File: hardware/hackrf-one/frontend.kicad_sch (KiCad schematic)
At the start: 150 parts, among them J10 GND_CLIP, J2 RF-SHIELD-FRAME, J3 RF-SHIELD-COVER, J4 MOUNTING_HOLE, J5 MOUNTING_HOLE, J6 MOUNTING_HOLE, J7 MOUNTING_HOLE, J8 MOUNTING_HOLE, J9 MOUNTING_HOLE, P13 GPO1, P17 GPO6, P19 GPO3, P21 REF_IN, P27 MIXER_SDATA, P31 MIXER_SCLK, P32 MIXER_ENX, P33 MIXER_RESETX, P34 MIX_BYPASS, P35 !MIX_BYPASS, P4 ANTENNA, P43 RX, P44 HP, P45 LP, P46 TX_MIX_BP, P47 RX_MIX_BP, P48 TX_AMP, P49 RX_AMP, P50 AMP_BYPASS, P51 !TX_AMP_PWR, P52 !RX_AMP_PWR, P6 GPO4, P7 GPO2, Q4 BSS84, T1 MIX_IN_BALUN, T2 MIX_OUT_BALUN, U1 SKY13453, U10 SKY13453, U11 SKY13453, U12 SKY13317, U13 TRF37B73, U14 SKY13317, U2 SKY13453, U25 TRF37B73, U3 RX_LOWPASS_FILTER, U4 RFFC5072, U5 SKY13453, U6 SKY13453, U7 SKY13453, U8 RX_HIGHPASS_FILTER, U9 SKY13317

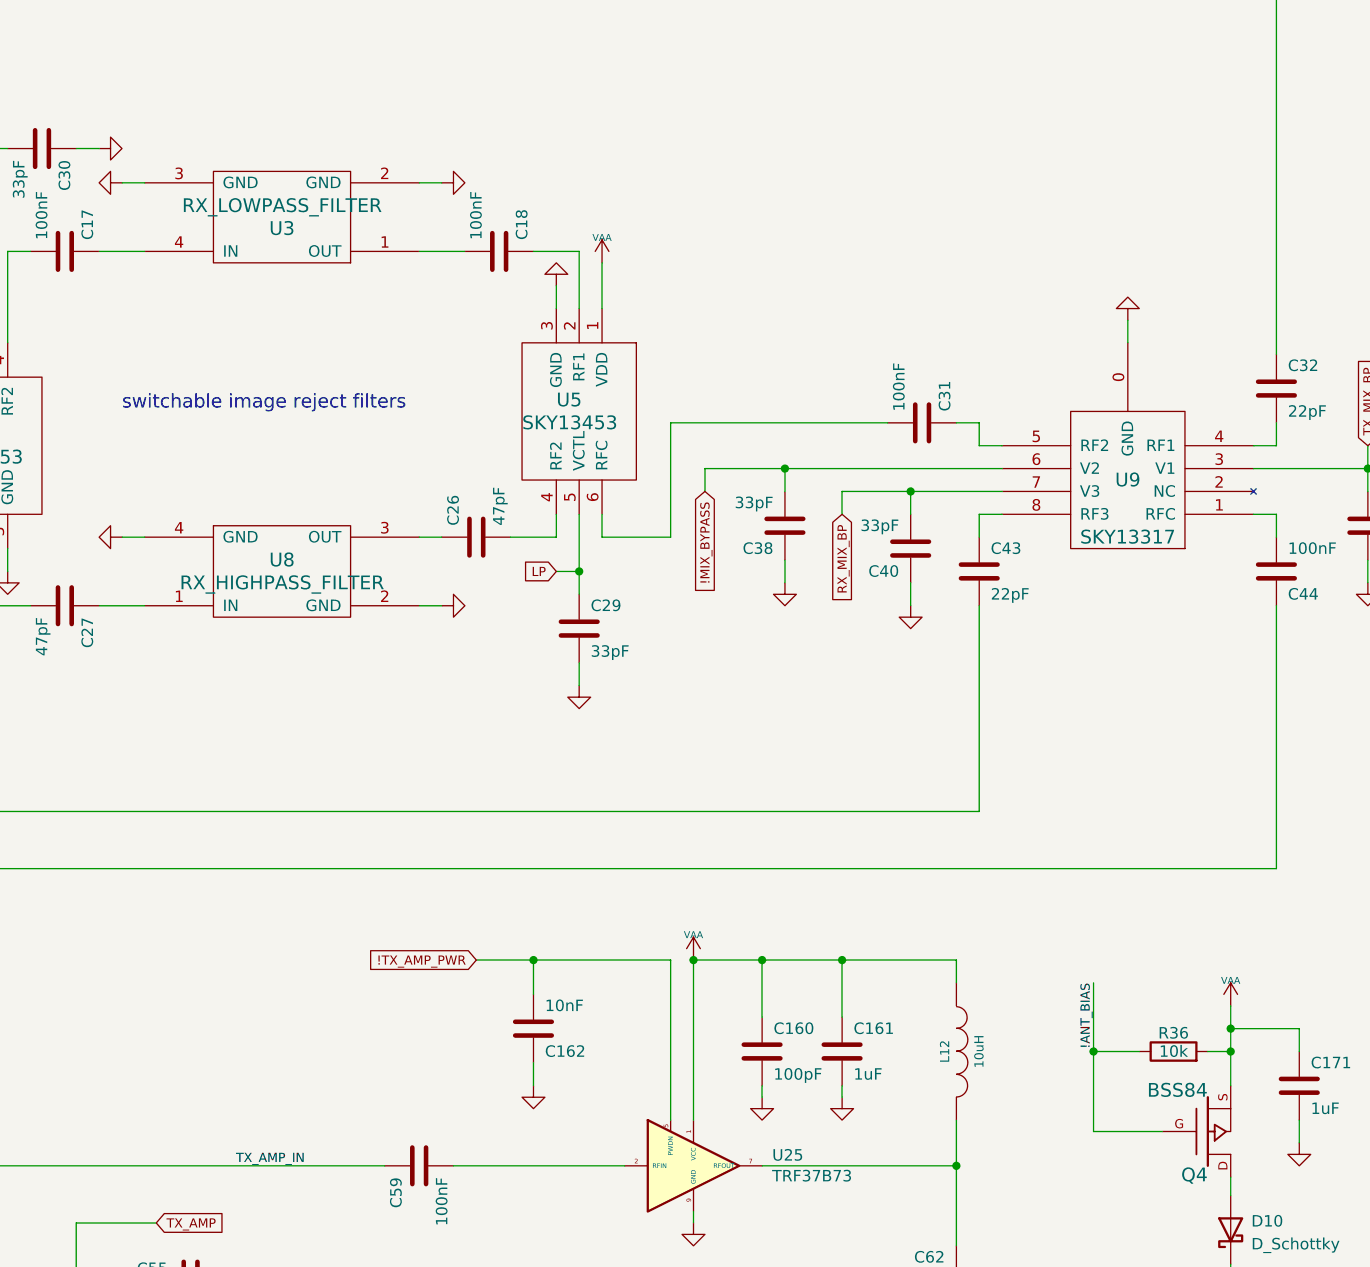
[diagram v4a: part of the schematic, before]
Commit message: Made design changes to indicate version 15. Correct Q3/4/5 part-no and LPF rotation
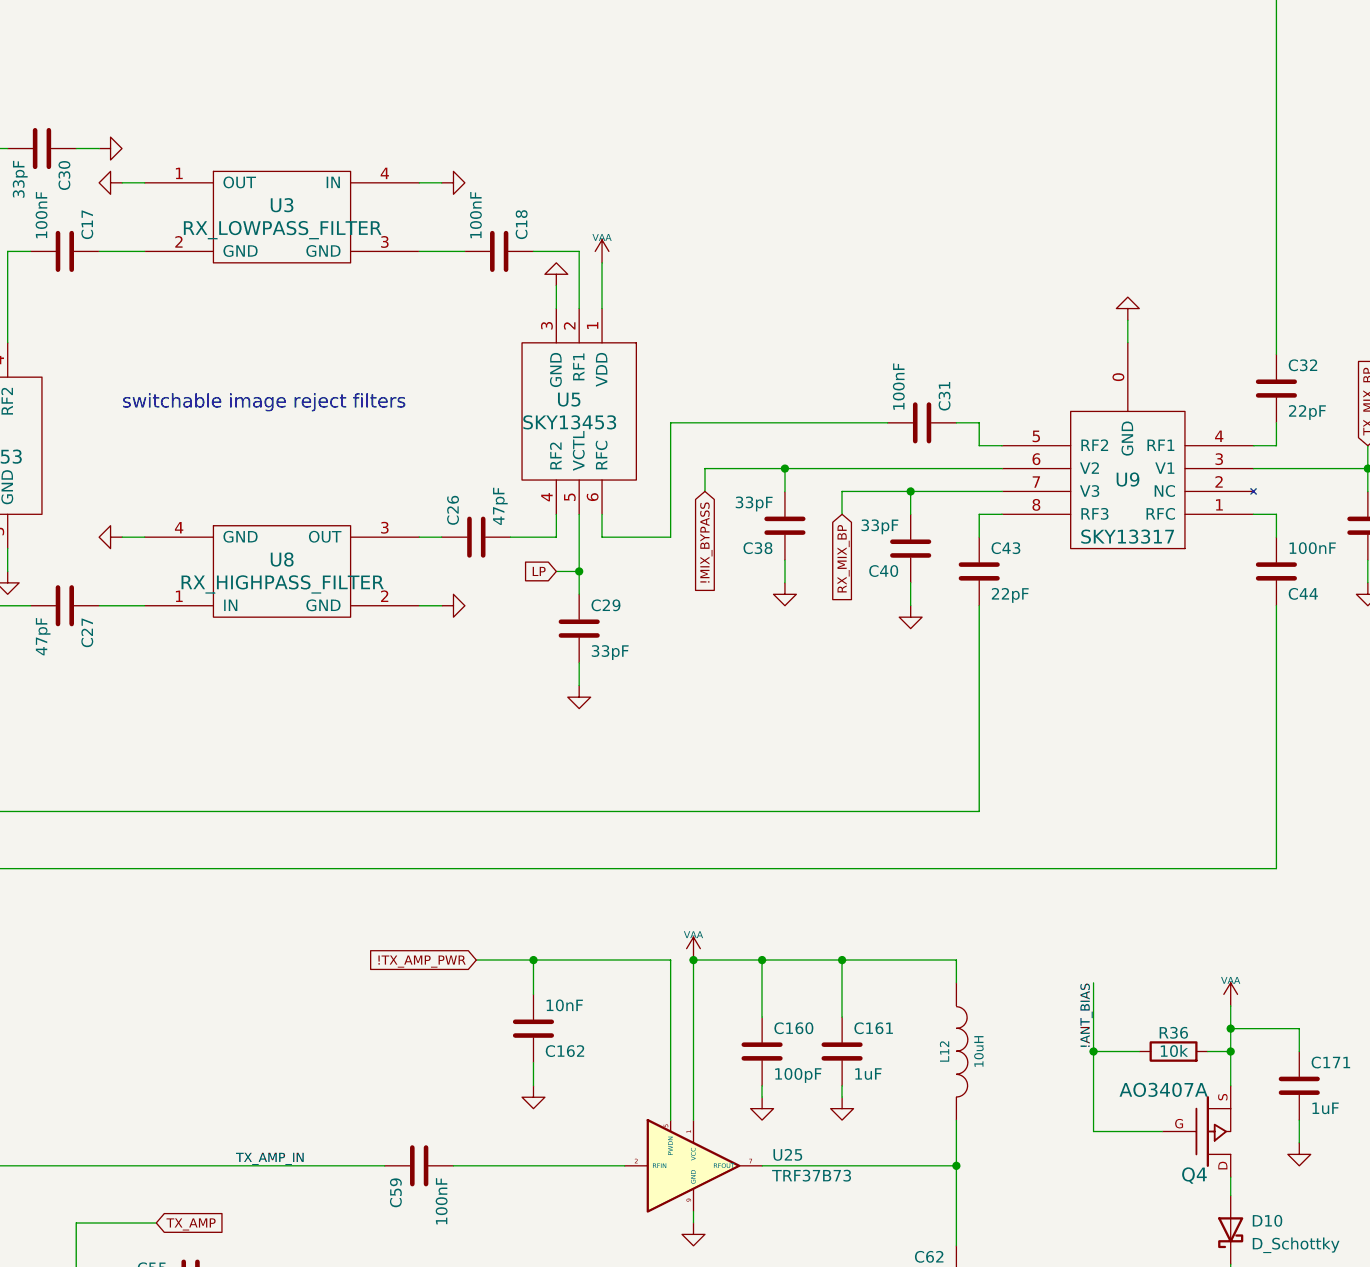
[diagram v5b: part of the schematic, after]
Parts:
- Q4: value BSS84 -> AO3407A; Manufacturer Fairchild -> Alpha and Omega; Part Number BSS84 -> AO3407A
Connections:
- net GND: now also U3.1 (OUT), U3.4 (IN); no longer U3.2 (GND), U3.3 (GND)
- net at C18.2: now also U3.3 (GND); no longer U3.1 (OUT)
- net at C17.1: now also U3.2 (GND); no longer U3.4 (IN)
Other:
- moved on the sheet: U3
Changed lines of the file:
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@@
 	(symbol
 		(lib_id "hackrf-one:FIL-LP0603-hackrf")
-		(at 289.56 58.42 180)
+		(at 289.56 58.42 0)
 		(unit 1)
 		(exclude_from_sim no)
@@
 		(dnp no)
 		(property "Reference" "U3"
-			(at 289.56 59.69 0)
+			(at 289.56 57.15 0)
 			(effects
 				(font
@@
 		)
 		(property "Value" "RX_LOWPASS_FILTER"
-			(at 289.56 57.15 0)
+			(at 289.56 59.69 0)
 			(effects
 				(font
@@
 			)
 		)
-		(property "Value" "BSS84"
+		(property "Value" "AO3407A"
 			(at 392.43 155.448 0)
 			(effects
@@
 			)
 		)
-		(property "Description" "MOSFET P-CH 50V 130MA SOT-23"
+		(property "Description" "MOSFET P-CH -30V -4.3A SOT23"
 			(at 392.43 160.02 0)
 			(effects
@@
 			)
 		)
-		(property "Manufacturer" "Fairchild"
+		(property "Manufacturer" "Alpha and Omega"
 			(at 392.43 160.02 0)
 			(effects
@@
 			)
 		)
-		(property "Part Number" "BSS84"
+		(property "Part Number" "AO3407A"
 			(at 392.43 160.02 0)
 			(effects

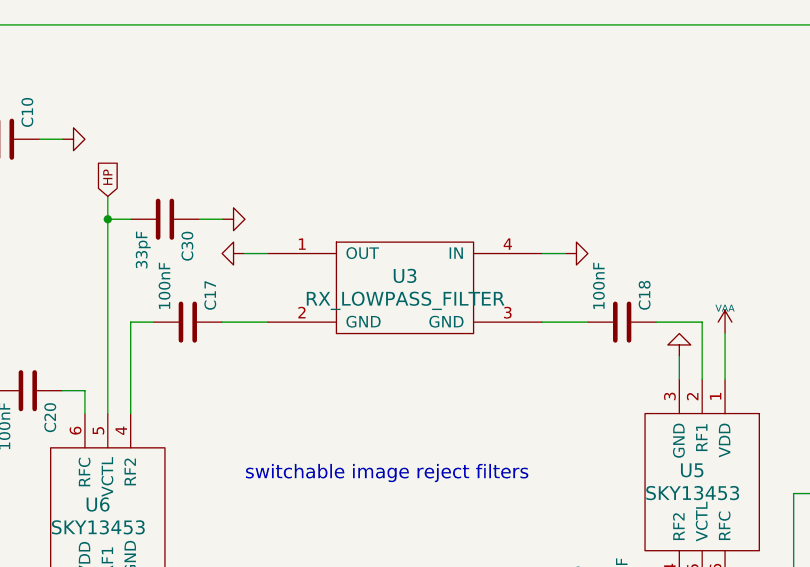
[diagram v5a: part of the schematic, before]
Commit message: Added U15 version detection resistors, corrected FETs and U3 rotation
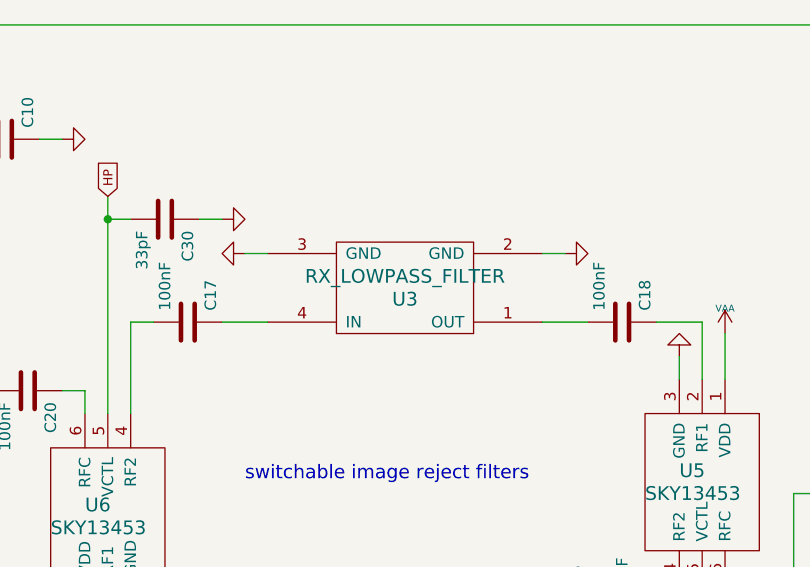
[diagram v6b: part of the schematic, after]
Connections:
- net GND: now also U3.2 (GND), U3.3 (GND); no longer U3.1 (OUT), U3.4 (IN)
- net at C17.1: now also U3.4 (IN); no longer U3.2 (GND)
- net at C18.2: now also U3.1 (OUT); no longer U3.3 (GND)
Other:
- moved on the sheet: U3
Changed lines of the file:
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@@
 	(symbol
 		(lib_id "hackrf-one:FIL-LP0603-hackrf")
-		(at 289.56 58.42 0)
+		(at 289.56 58.42 180)
 		(unit 1)
 		(exclude_from_sim no)
@@
 		(dnp no)
 		(property "Reference" "U3"
-			(at 289.56 57.15 0)
+			(at 289.56 59.69 0)
 			(effects
 				(font
@@
 		)
 		(property "Value" "RX_LOWPASS_FILTER"
-			(at 289.56 59.69 0)
+			(at 289.56 57.15 0)
 			(effects
 				(font
